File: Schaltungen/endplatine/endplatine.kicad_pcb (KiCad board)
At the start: 2 copper layers, 38 parts, among them P1 CONN_5X2, Q1 BC337, Q2 BC337, SW1 SW_PUSH, T1 BC337, T2 BC307, U1 LM358N

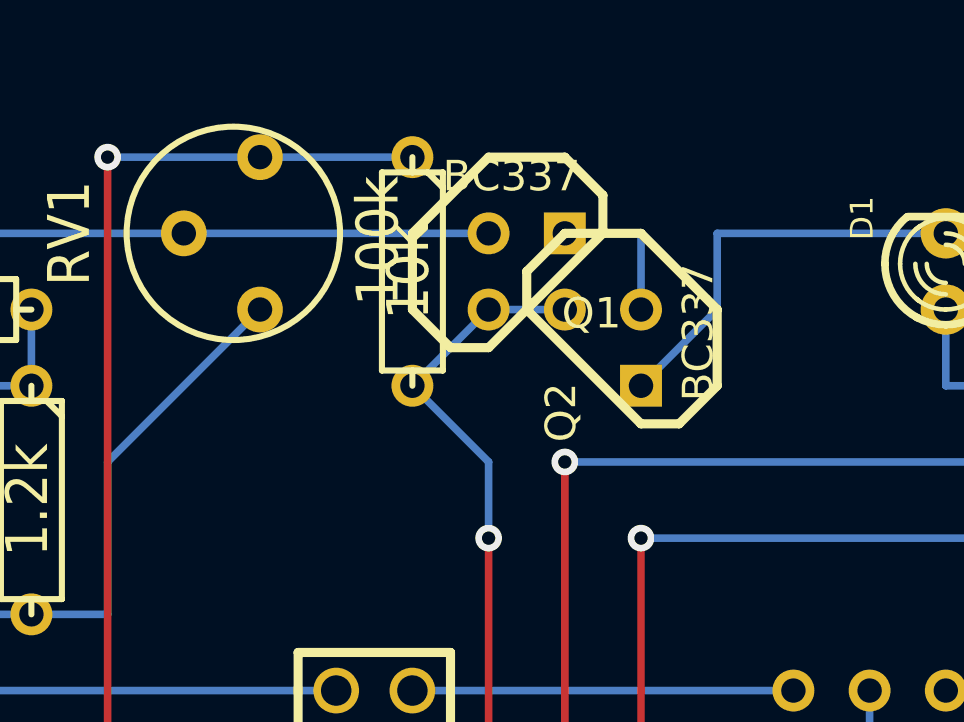
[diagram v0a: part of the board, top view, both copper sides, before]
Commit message: Firmware für Endplatine angefangen, kleine Änderungen am Platinenentwurf.
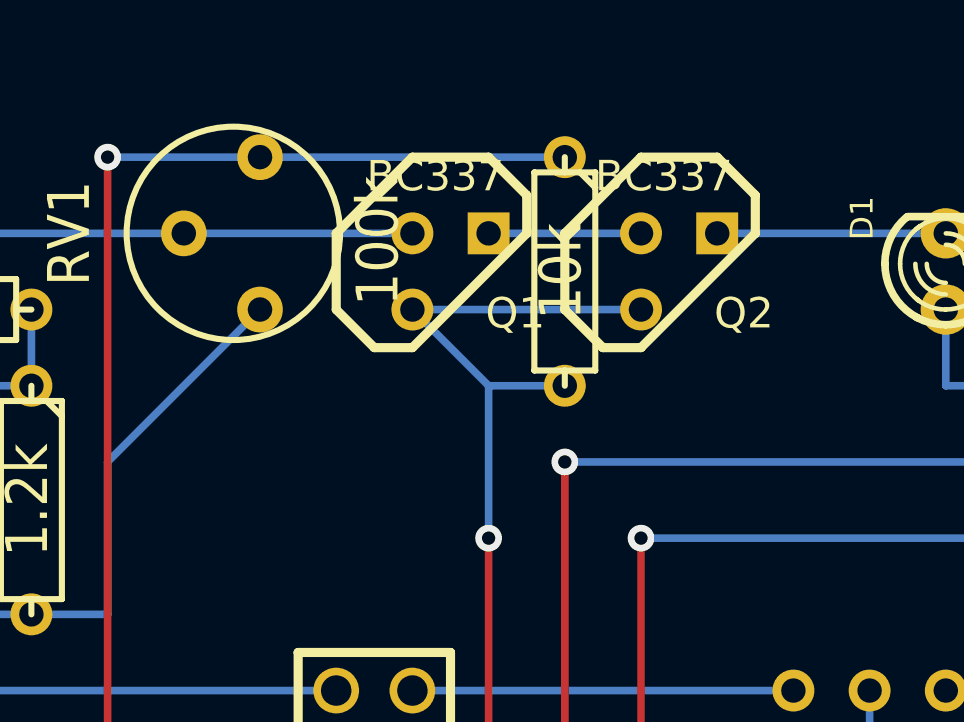
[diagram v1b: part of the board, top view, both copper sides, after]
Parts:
- moved R11 5.08 mm to (68.6, 87.6)
- moved Q2 3.59 mm to (72.4, 87.6), turned to 0 degrees
- moved Q1 2.54 mm to (64.8, 87.6)
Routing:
- net /Mikrocontroller/Empfänger/Signal: track 79.4 -> 85.9 mm
- net GND: track 211.6 -> 205.5 mm
- net +5V: track 94.0 -> 99.1 mm
- net N-0000044: track 20.3 -> 17.8 mm
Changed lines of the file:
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@@
     (links 78)
     (no_connects 3)
-    (area 14.7828 77.368399 162.435116 151.80945)
+    (area 14.7828 80.3275 112.204501 122.047001)
     (thickness 1.6)
     (drawings 0)
-    (tracks 164)
+    (tracks 162)
     (zones 0)
     (modules 38)
@@
   )
   (module TO92-EBC (layer F.Cu)
-    (at 67.31 87.63)
+    (at 64.77 87.63)
     (descr "Transistor TO92 brochage type BC237")
     (tags "TR TO92")
@@
   )
   (module TO92-EBC (layer F.Cu)
-    (at 69.85 90.17 270)
+    (at 72.39 87.63)
     (descr "Transistor TO92 brochage type BC237")
     (tags "TR TO92")
-    (fp_text reference Q2 (at 2.159 1.397 270) (layer F.SilkS)
-      (effects (font (size 1.016 1.016) (thickness 0.2032)))
-    )
-    (fp_text value BC337 (at -0.508 -3.175 270) (layer F.SilkS)
+    (fp_text reference Q2 (at 2.159 1.397) (layer F.SilkS)
+      (effects (font (size 1.016 1.016) (thickness 0.2032)))
+    )
+    (fp_text value BC337 (at -0.508 -3.175) (layer F.SilkS)
       (effects (font (size 1.016 1.016) (thickness 0.2032)))
     )
@@
     (fp_line (start -3.81 1.27) (end -2.54 2.54) (layer F.SilkS) (width 0.3048))
     (fp_line (start -2.54 2.54) (end -1.27 2.54) (layer F.SilkS) (width 0.3048))
-    (pad E thru_hole rect (at 1.27 -1.27 270) (size 1.397 1.397) (drill 0.8128)
-      (layers *.Cu *.Mask F.SilkS)
-      (net 6 GND)
-    )
-    (pad B thru_hole circle (at -1.27 -1.27 270) (size 1.397 1.397) (drill 0.8128)
+    (pad E thru_hole rect (at 1.27 -1.27) (size 1.397 1.397) (drill 0.8128)
+      (layers *.Cu *.Mask F.SilkS)
+      (net 6 GND)
+    )
+    (pad B thru_hole circle (at -1.27 -1.27) (size 1.397 1.397) (drill 0.8128)
       (layers *.Cu *.Mask F.SilkS)
       (net 24 N-0000041)
     )
-    (pad C thru_hole circle (at -1.27 1.27 270) (size 1.397 1.397) (drill 0.8128)
+    (pad C thru_hole circle (at -1.27 1.27) (size 1.397 1.397) (drill 0.8128)
       (layers *.Cu *.Mask F.SilkS)
       (net 4 /Mikrocontroller/Empfänger/Signal)
@@
   )
   (module R3 (layer F.Cu)
-    (at 63.5 87.63 270)
+    (at 68.58 87.63 270)
     (descr "Resitance 3 pas")
     (tags R)
@@
   (segment (start 53.34 114.3) (end 53.34 83.82) (width 0.254) (layer F.Cu) (net 2))
   (segment (start 53.34 114.3) (end 53.34 114.3) (width 0.254) (layer F.Cu) (net 2))
-  (segment (start 63.5 83.82) (end 58.42 83.82) (width 0.254) (layer B.Cu) (net 2))
+  (segment (start 68.58 83.82) (end 58.42 83.82) (width 0.254) (layer B.Cu) (net 2) (status C00000))
   (segment (start 86.36 114.3) (end 91.44 114.3) (width 0.254) (layer B.Cu) (net 2))
   (segment (start 91.44 114.3) (end 91.44 111.76) (width 0.254) (layer B.Cu) (net 2))
@@
   (segment (start 33.02 101.6) (end 33.02 96.52) (width 0.254) (layer F.Cu) (net 3))
   (via (at 33.02 101.6) (size 0.889) (layers F.Cu B.Cu) (net 3))
-  (segment (start 63.5 91.44) (end 66.04 93.98) (width 0.254) (layer B.Cu) (net 4))
+  (segment (start 68.58 91.44) (end 66.04 91.44) (width 0.254) (layer B.Cu) (net 4) (status 400000))
+  (segment (start 63.5 88.9) (end 66.04 91.44) (width 0.254) (layer B.Cu) (net 4) (status 400000))
   (segment (start 88.9 121.92) (end 88.9 109.22) (width 0.254) (layer F.Cu) (net 4))
   (segment (start 66.04 121.92) (end 88.9 121.92) (width 0.254) (layer F.Cu) (net 4))
   (segment (start 66.04 96.52) (end 66.04 121.92) (width 0.254) (layer F.Cu) (net 4))
   (via (at 66.04 96.52) (size 0.889) (layers F.Cu B.Cu) (net 4))
-  (segment (start 66.04 93.98) (end 66.04 96.52) (width 0.254) (layer B.Cu) (net 4))
+  (segment (start 66.04 91.44) (end 66.04 96.52) (width 0.254) (layer B.Cu) (net 4))
   (via (at 88.9 109.22) (size 0.889) (layers F.Cu B.Cu) (net 4))
   (segment (start 88.9 109.22) (end 87.63 110.49) (width 0.254) (layer B.Cu) (net 4))
   (segment (start 85.09 110.49) (end 83.82 109.22) (width 0.254) (layer B.Cu) (net 4))
   (segment (start 87.63 110.49) (end 85.09 110.49) (width 0.254) (layer B.Cu) (net 4))
-  (segment (start 63.5 91.44) (end 66.04 88.9) (width 0.254) (layer B.Cu) (net 4))
-  (segment (start 66.04 88.9) (end 68.58 88.9) (width 0.254) (layer B.Cu) (net 4))
+  (segment (start 63.5 88.9) (end 66.04 88.9) (width 0.254) (layer B.Cu) (net 4) (status 400000))
+  (segment (start 66.04 88.9) (end 71.12 88.9) (width 0.254) (layer B.Cu) (net 4) (status 800000))
   (segment (start 106.68 101.6) (end 106.68 99.06) (width 0.254) (layer B.Cu) (net 5))
   (segment (start 111.76 119.38) (end 55.88 119.38) (width 0.254) (layer B.Cu) (net 5))
   (segment (start 111.76 99.06) (end 111.76 119.38) (width 0.254) (layer B.Cu) (net 5))
   (segment (start 106.68 99.06) (end 111.76 99.06) (width 0.254) (layer B.Cu) (net 5))
+  (segment (start 73.66 86.36) (end 81.28 86.36) (width 0.254) (layer B.Cu) (net 6) (status C00000))
   (segment (start 50.8 106.68) (end 43.18 106.68) (width 0.254) (layer B.Cu) (net 6))
-  (segment (start 43.18 106.68) (end 43.18 111.76) (width 0.254) (layer F.Cu) (net 6) (status 800000))
+  (segment (start 43.18 106.68) (end 43.18 111.76) (width 0.254) (layer F.Cu) (net 6))
   (via (at 43.18 106.68) (size 0.889) (layers F.Cu B.Cu) (net 6))
   (via (at 55.88 106.68) (size 0.889) (layers F.Cu B.Cu) (net 6))
@@
   (via (at 55.88 116.84) (size 0.889) (layers F.Cu B.Cu) (net 6))
   (segment (start 55.88 116.84) (end 55.88 106.68) (width 0.254) (layer F.Cu) (net 6))
-  (segment (start 71.12 91.44) (end 73.66 88.9) (width 0.254) (layer B.Cu) (net 6))
-  (segment (start 73.66 86.36) (end 81.28 86.36) (width 0.254) (layer B.Cu) (net 6))
-  (segment (start 73.66 88.9) (end 73.66 86.36) (width 0.254) (layer B.Cu) (net 6))
   (segment (start 81.28 86.36) (end 86.36 86.36) (width 0.254) (layer B.Cu) (net 6))
   (segment (start 86.36 86.36) (end 91.44 86.36) (width 0.254) (layer B.Cu) (net 6))
@@
   (segment (start 88.9 99.06) (end 88.9 101.6) (width 0.254) (layer B.Cu) (net 14))
   (segment (start 17.78 109.22) (end 25.4 109.22) (width 0.254) (layer B.Cu) (net 15))
-  (segment (start 45.72 109.22) (end 48.26 109.22) (width 0.254) (layer B.Cu) (net 16) (status C00000))
+  (segment (start 45.72 109.22) (end 48.26 109.22) (width 0.254) (layer B.Cu) (net 16))
   (segment (start 27.94 104.14) (end 27.94 109.22) (width 0.254) (layer B.Cu) (net 16))
   (segment (start 27.94 109.22) (end 45.72 109.22) (width 0.254) (layer B.Cu) (net 16))
@@
   (segment (start 34.29 115.57) (end 33.02 116.84) (width 0.254) (layer B.Cu) (net 17))
   (segment (start 34.29 113.03) (end 34.29 115.57) (width 0.254) (layer B.Cu) (net 17))
-  (segment (start 45.72 111.76) (end 48.26 111.76) (width 0.254) (layer B.Cu) (net 18) (status 400000))
-  (segment (start 48.26 111.76) (end 48.26 116.84) (width 0.254) (layer B.Cu) (net 18) (status 800000))
-  (segment (start 48.26 116.84) (end 48.26 119.38) (width 0.254) (layer B.Cu) (net 18) (status C00000))
+  (segment (start 45.72 111.76) (end 48.26 111.76) (width 0.254) (layer B.Cu) (net 18))
+  (segment (start 48.26 111.76) (end 48.26 116.84) (width 0.254) (layer B.Cu) (net 18))
+  (segment (start 48.26 116.84) (end 48.26 119.38) (width 0.254) (layer B.Cu) (net 18))
   (segment (start 25.4 114.3) (end 25.4 116.84) (width 0.254) (layer B.Cu) (net 19))
   (segment (start 25.4 116.84) (end 25.4 119.38) (width 0.254) (layer B.Cu) (net 19))
@@
   (segment (start 43.18 88.9) (end 43.18 86.36) (width 0.254) (layer B.Cu) (net 23))
   (segment (start 38.1 88.9) (end 43.18 88.9) (width 0.254) (layer B.Cu) (net 23))
-  (segment (start 68.58 86.36) (end 71.12 86.36) (width 0.254) (layer B.Cu) (net 24))
-  (segment (start 71.12 86.36) (end 71.12 88.9) (width 0.254) (layer B.Cu) (net 24))
+  (segment (start 66.04 86.36) (end 71.12 86.36) (width 0.254) (layer B.Cu) (net 24) (status C00000))
   (segment (start 50.8 91.44) (end 38.1 91.44) (width 0.254) (layer B.Cu) (net 25))
   (segment (start 50.8 88.9) (end 50.8 91.44) (width 0.254) (layer B.Cu) (net 25))
@@
   (segment (start 17.78 93.98) (end 20.32 91.44) (width 0.254) (layer B.Cu) (net 26))
   (segment (start 20.32 91.44) (end 30.48 91.44) (width 0.254) (layer B.Cu) (net 26))
+  (segment (start 55.88 86.36) (end 63.5 86.36) (width 0.254) (layer B.Cu) (net 27) (status C00000))
   (segment (start 45.72 86.36) (end 55.88 86.36) (width 0.254) (layer B.Cu) (net 27))
-  (segment (start 55.88 86.36) (end 66.04 86.36) (width 0.254) (layer B.Cu) (net 27))
   (segment (start 43.18 96.52) (end 43.18 93.98) (width 0.254) (layer B.Cu) (net 28))
   (segment (start 43.18 93.98) (end 45.72 93.98) (width 0.254) (layer B.Cu) (net 28))

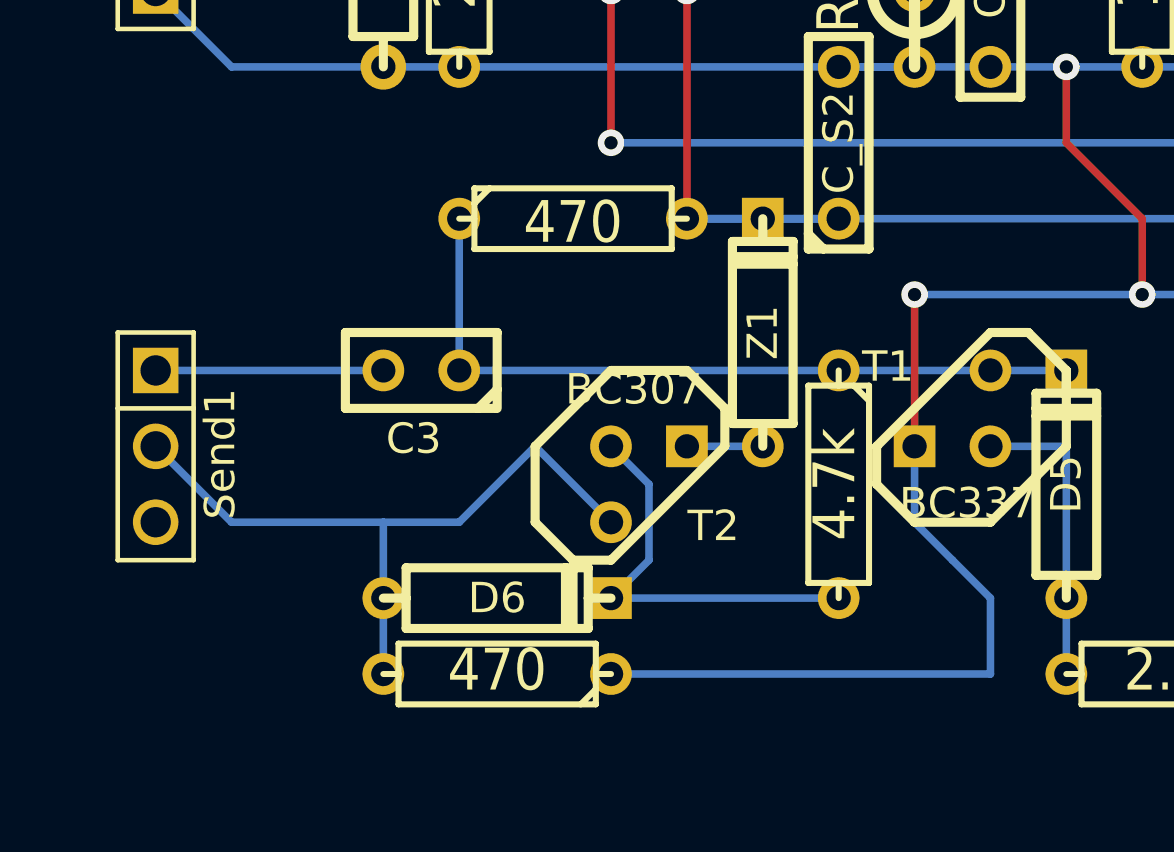
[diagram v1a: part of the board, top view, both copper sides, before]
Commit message: platinenlayout an überarbeiteten Verstärker angepasst. Wenn das nicht klappt -> Extra TreiberIC o.ä.
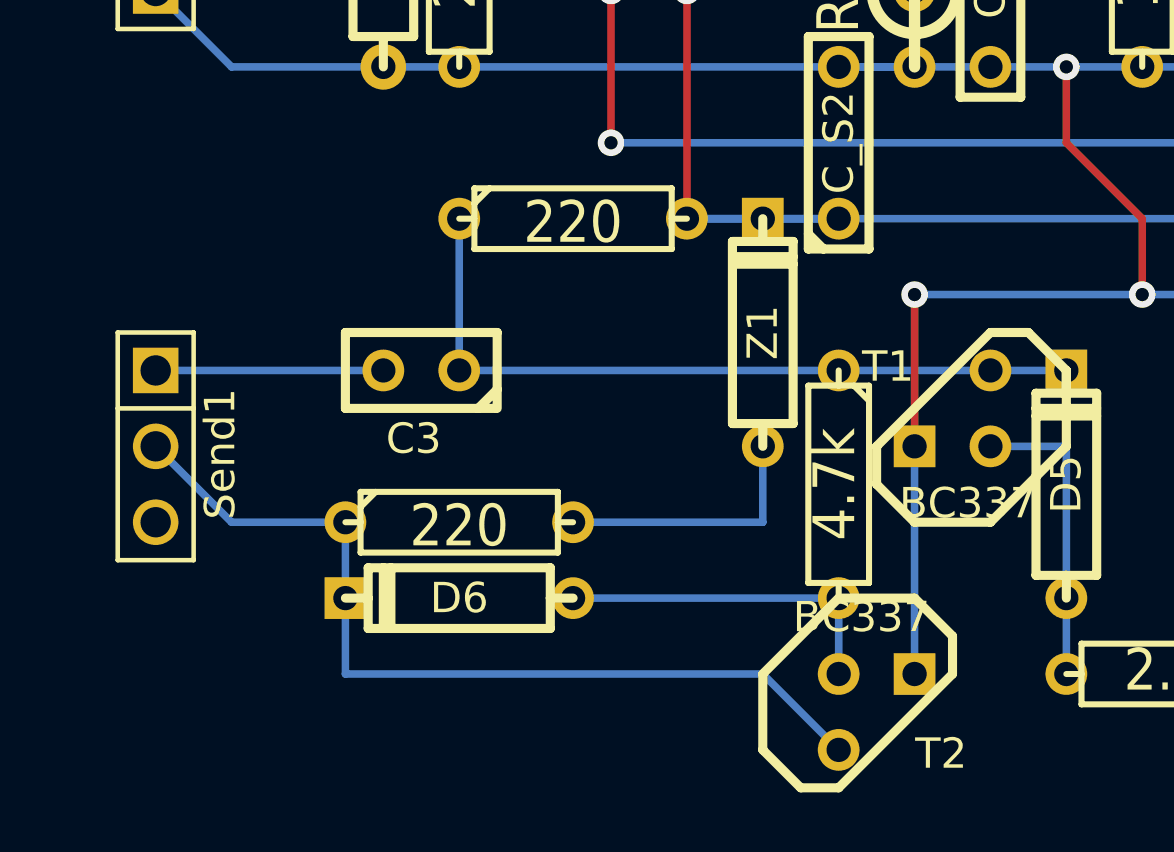
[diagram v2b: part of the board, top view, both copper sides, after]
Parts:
- R12, R13: value 470 -> 220
- T2: value BC307 -> BC337
- moved T2 10.8 mm to (41.9, 120.7)
- moved R13 5.24 mm to (27.9, 114.3), turned to 0 degrees
- moved D6 1.27 mm to (27.9, 116.8), turned to 180 degrees
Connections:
- D6 pad 1: N-0000036 -> N-0000037
- D6 pad 2: N-0000034 (its old number) -> N-0000036
- R13 pad 1: GND -> N-0000036
- R13 pad 2: N-0000036 -> N-0000033
- RB2 pad 2: N-0000034 (its old number) -> N-0000037
- T2 pad B: N-0000034 (its old number) -> N-0000037
- T2 pad E: N-0000037 -> GND
- Z1 pad 1: N-0000037 -> N-0000033
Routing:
- net N-0000034 (its old number): track 13.8 -> 0.00 mm
- net GND: track 205.5 -> 191.7 mm
- net N-0000037: track 2.54 -> 11.4 mm
- net N-0000033: track 0.00 -> 8.89 mm
- net N-0000036: track 23.5 -> 30.0 mm
